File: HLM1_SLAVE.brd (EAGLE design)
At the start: 47.9 x 63.5 mm, 7 parts

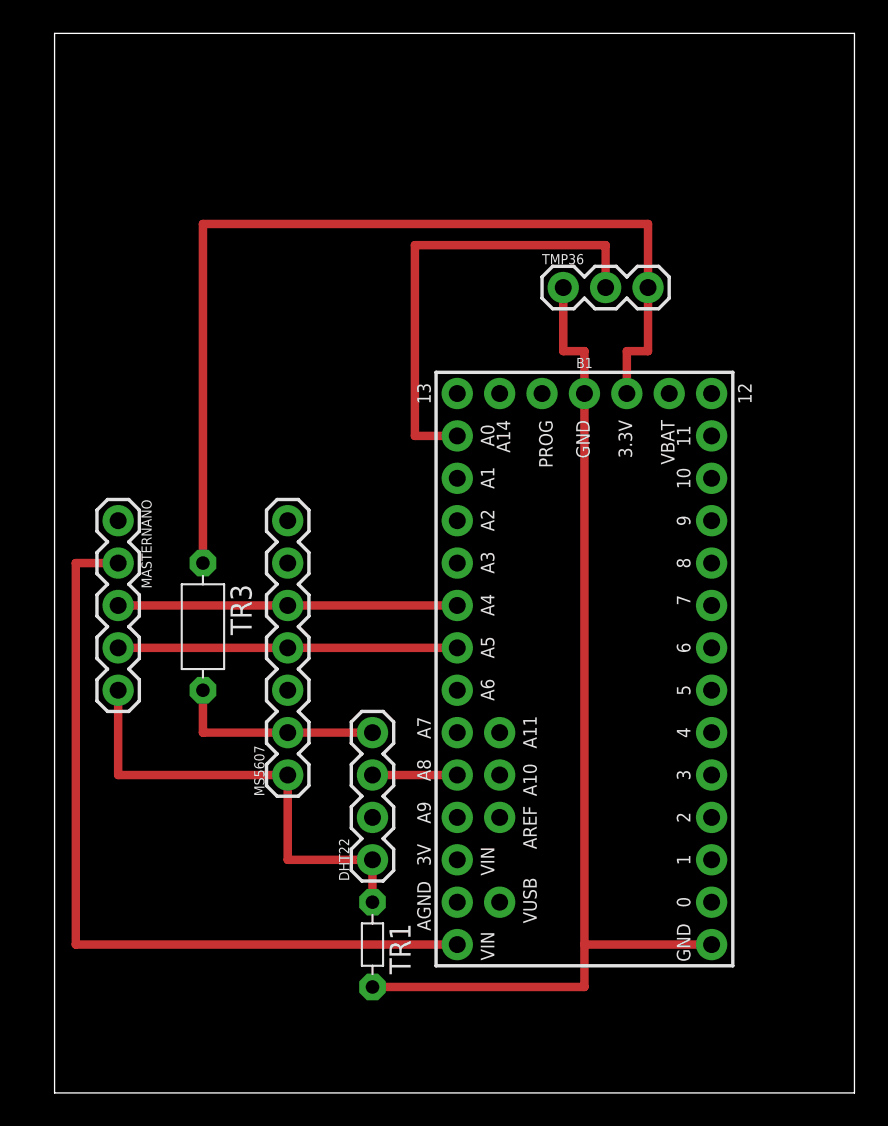
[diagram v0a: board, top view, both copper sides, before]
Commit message: Connected I2C lines to slave device for board carving
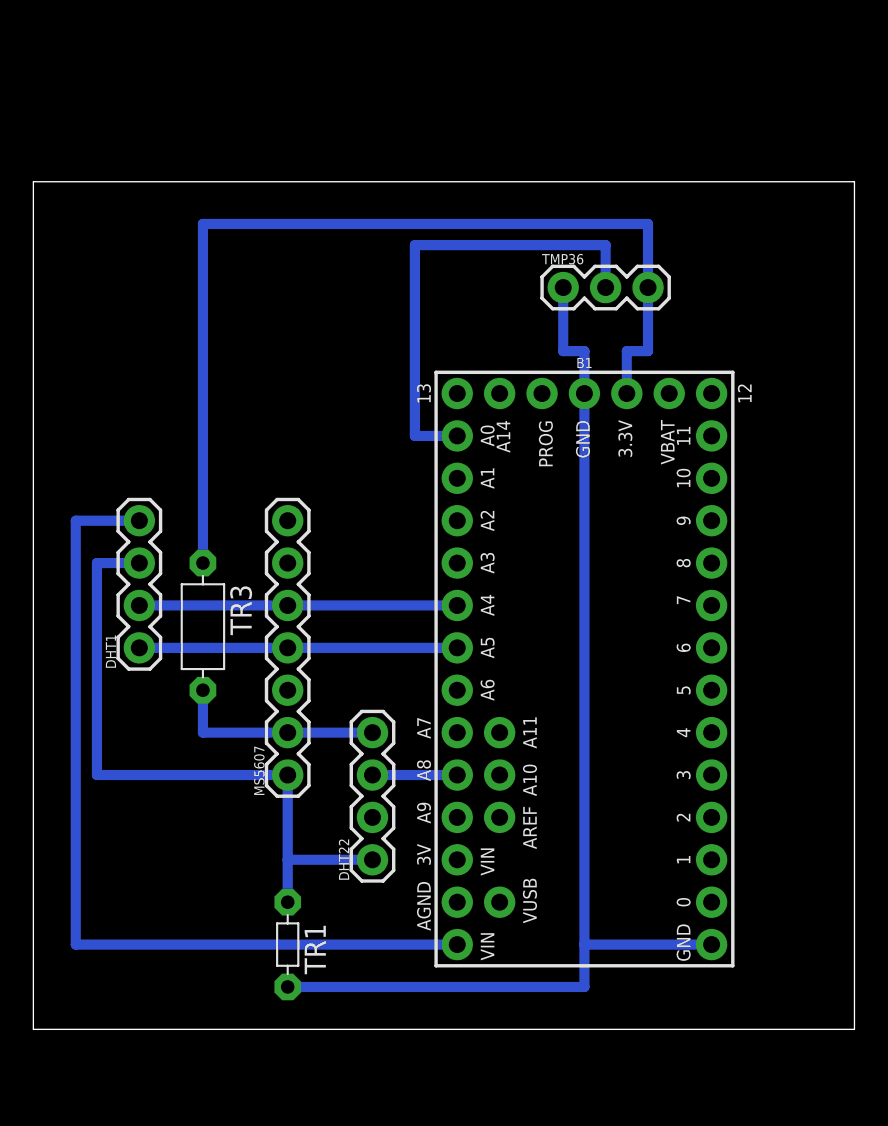
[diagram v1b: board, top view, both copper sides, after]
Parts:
- removed MASTERNANO: (no value), SparkFun-Connectors:1X05
- added DHT1: (no value), SparkFun-Connectors:1X04
- moved TR1 5.08 mm to (33.0, 16.5)
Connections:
- removed net 5V: MASTERNANO.1
- net GND: now also DHT1.3; no longer MASTERNANO.5
- net SCL: now also DHT1.1; no longer MASTERNANO.4
- net SDA: now also DHT1.2; no longer MASTERNANO.3
- net VIN: now also DHT1.4; no longer MASTERNANO.2
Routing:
- net GND: track 91.4 -> 107.9 mm
- net VIN: track 48.3 -> 52.1 mm
- net SDA: track 20.3 -> 19.1 mm
- net SCL: track 20.3 -> 19.1 mm
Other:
- board size 47.9 x 63.5 mm -> 49.2 x 50.8 mm
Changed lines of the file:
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@@
 <?xml version="1.0" encoding="utf-8"?>
 <!DOCTYPE eagle SYSTEM "eagle.dtd">
-<eagle version="8.5.1">
+<eagle version="9.0.1">
 <drawing>
 <settings>
@@
 <board>
 <plain>
-<wire x1="19.05" y1="7.62" x2="66.98" y2="7.62" width="0" layer="20"/>
-<wire x1="66.98" y1="7.62" x2="66.98" y2="71.11" width="0" layer="20"/>
-<wire x1="66.98" y1="71.11" x2="19.05" y2="71.11" width="0" layer="20"/>
-<wire x1="19.05" y1="71.11" x2="19.05" y2="7.62" width="0" layer="20"/>
+<wire x1="17.78" y1="11.43" x2="66.98" y2="11.43" width="0" layer="20"/>
+<wire x1="66.98" y1="11.43" x2="66.98" y2="62.22" width="0" layer="20"/>
+<wire x1="66.98" y1="62.22" x2="17.78" y2="62.22" width="0" layer="20"/>
+<wire x1="17.78" y1="62.22" x2="17.78" y2="11.43" width="0" layer="20"/>
 <text x="35.56" y="62.23" size="1.778" layer="27">+</text>
 </plain>
@@
 </element>
 <element name="MS5607" library="SparkFun-Connectors" package="1X07" value="" x="33.02" y="26.67" rot="R90"/>
-<element name="MASTERNANO" library="SparkFun-Connectors" package="1X05" value="" x="22.86" y="41.91" rot="R270"/>
-<element name="TR1" library="discrete" library_urn="urn:adsk.eagle:library:211" package="R-5" package3d_urn="urn:adsk.eagle:package:12931/1" value="" x="38.1" y="16.51" rot="R270"/>
+<element name="TR1" library="discrete" library_urn="urn:adsk.eagle:library:211" package="R-5" package3d_urn="urn:adsk.eagle:package:12931/1" value="" x="33.02" y="16.51" rot="R270"/>
 <element name="TR3" library="discrete" library_urn="urn:adsk.eagle:library:211" package="R-7,5" package3d_urn="urn:adsk.eagle:package:12930/1" value="" x="27.94" y="35.56" rot="R270"/>
+<element name="DHT1" library="SparkFun-Connectors" package="1X04" value="" x="24.13" y="34.29" rot="R90">
+<attribute name="PROD_ID" value="CONN-09696" x="24.13" y="34.29" size="1.778" layer="27" rot="R90" display="off"/>
+</element>
 </elements>
 <signals>
@@
 </signal>
 <signal name="GND">
-<contactref element="MASTERNANO" pad="5"/>
 <contactref element="DHT22" pad="1"/>
 <contactref element="B1" pad="GND"/>
@@
 <contactref element="MS5607" pad="1"/>
 <contactref element="B1" pad="GND1"/>
-<wire x1="49.53" y1="55.88" x2="49.53" y2="52.07" width="0.508" layer="1"/>
-<wire x1="49.53" y1="52.07" x2="50.8" y2="52.07" width="0.508" layer="1"/>
-<wire x1="50.8" y1="52.07" x2="50.8" y2="49.53" width="0.508" layer="1"/>
-<wire x1="38.1" y1="21.59" x2="33.02" y2="21.59" width="0.508" layer="1"/>
-<wire x1="33.02" y1="21.59" x2="33.02" y2="26.67" width="0.508" layer="1"/>
-<wire x1="33.02" y1="26.67" x2="22.86" y2="26.67" width="0.508" layer="1"/>
-<wire x1="22.86" y1="26.67" x2="22.86" y2="31.75" width="0.508" layer="1"/>
+<wire x1="49.53" y1="55.88" x2="49.53" y2="52.07" width="0.6096" layer="16"/>
+<wire x1="49.53" y1="52.07" x2="50.8" y2="52.07" width="0.6096" layer="16"/>
+<wire x1="50.8" y1="52.07" x2="50.8" y2="49.53" width="0.6096" layer="16"/>
+<wire x1="38.1" y1="21.59" x2="33.02" y2="21.59" width="0.6096" layer="16"/>
+<wire x1="33.02" y1="21.59" x2="33.02" y2="26.67" width="0.6096" layer="16"/>
 <contactref element="TR1" pad="2"/>
 <contactref element="TR1" pad="1"/>
-<wire x1="38.1" y1="21.59" x2="38.1" y2="19.05" width="0.508" layer="1"/>
-<wire x1="58.42" y1="16.51" x2="50.8" y2="16.51" width="0.508" layer="1"/>
-<wire x1="50.8" y1="16.51" x2="50.8" y2="49.53" width="0.508" layer="1"/>
-<wire x1="38.1" y1="13.97" x2="50.8" y2="13.97" width="0.508" layer="1"/>
-<wire x1="50.8" y1="13.97" x2="50.8" y2="16.51" width="0.508" layer="1"/>
-<wire x1="38.1" y1="19.05" x2="38.1" y2="13.97" width="0" layer="19" extent="1-1"/>
+<wire x1="58.42" y1="16.51" x2="50.8" y2="16.51" width="0.6096" layer="16"/>
+<wire x1="50.8" y1="16.51" x2="50.8" y2="49.53" width="0.6096" layer="16"/>
+<wire x1="33.02" y1="13.97" x2="50.8" y2="13.97" width="0.6096" layer="16"/>
+<wire x1="50.8" y1="13.97" x2="50.8" y2="16.51" width="0.6096" layer="16"/>
+<contactref element="DHT1" pad="3"/>
+<wire x1="21.59" y1="26.67" x2="21.59" y2="39.37" width="0.6096" layer="16"/>
+<wire x1="21.59" y1="39.37" x2="24.13" y2="39.37" width="0.6096" layer="16"/>
+<wire x1="33.02" y1="26.67" x2="21.59" y2="26.67" width="0.6096" layer="16"/>
+<wire x1="33.02" y1="19.05" x2="33.02" y2="21.59" width="0.6096" layer="16"/>
+<wire x1="33.02" y1="19.05" x2="33.02" y2="13.97" width="0" layer="19" extent="1-1"/>
 </signal>
 <signal name="SDA">
-<contactref element="MASTERNANO" pad="3"/>
+<contactref element="MS5607" pad="5"/>
+<contactref element="DHT1" pad="2"/>
+<wire x1="24.13" y1="36.83" x2="33.02" y2="36.83" width="0.6096" layer="16"/>
 <contactref element="B1" pad="18"/>
-<contactref element="MS5607" pad="5"/>
-<wire x1="33.02" y1="36.83" x2="43.18" y2="36.83" width="0.508" layer="1"/>
-<wire x1="22.86" y1="36.83" x2="33.02" y2="36.83" width="0.508" layer="1"/>
+<wire x1="33.02" y1="36.83" x2="43.18" y2="36.83" width="0.6096" layer="16"/>
 </signal>
 <signal name="SCL">
-<contactref element="MASTERNANO" pad="4"/>
+<contactref element="MS5607" pad="4"/>
+<contactref element="DHT1" pad="1"/>
+<wire x1="24.13" y1="34.29" x2="33.02" y2="34.29" width="0.6096" layer="16"/>
 <contactref element="B1" pad="19"/>
-<contactref element="MS5607" pad="4"/>
-<wire x1="33.02" y1="34.29" x2="43.18" y2="34.29" width="0.508" layer="1"/>
-<wire x1="22.86" y1="34.29" x2="33.02" y2="34.29" width="0.508" layer="1"/>
-</signal>
-<signal name="5V">
-<contactref element="MASTERNANO" pad="1"/>
+<wire x1="33.02" y1="34.29" x2="43.18" y2="34.29" width="0.6096" layer="16"/>
 </signal>
 <signal name="22">
 <contactref element="DHT22" pad="3"/>
 <contactref element="B1" pad="22"/>
-<wire x1="38.1" y1="26.67" x2="43.18" y2="26.67" width="0.508" layer="1"/>
+<wire x1="38.1" y1="26.67" x2="43.18" y2="26.67" width="0.6096" layer="16"/>
 </signal>
 <signal name="A0">
 <contactref element="TMP36" pad="2"/>
 <contactref element="B1" pad="14"/>
-<wire x1="52.07" y1="55.88" x2="52.07" y2="58.42" width="0.508" layer="1"/>
-<wire x1="52.07" y1="58.42" x2="40.64" y2="58.42" width="0.508" layer="1"/>
-<wire x1="40.64" y1="58.42" x2="40.64" y2="46.99" width="0.508" layer="1"/>
-<wire x1="40.64" y1="46.99" x2="43.18" y2="46.99" width="0.508" layer="1"/>
+<wire x1="52.07" y1="55.88" x2="52.07" y2="58.42" width="0.6096" layer="16"/>
+<wire x1="52.07" y1="58.42" x2="40.64" y2="58.42" width="0.6096" layer="16"/>
+<wire x1="40.64" y1="58.42" x2="40.64" y2="46.99" width="0.6096" layer="16"/>
+<wire x1="40.64" y1="46.99" x2="43.18" y2="46.99" width="0.6096" layer="16"/>
 </signal>
 <signal name="3V3">
@@
 <contactref element="TMP36" pad="3"/>
 <contactref element="DHT22" pad="4"/>
-<wire x1="54.61" y1="55.88" x2="54.61" y2="52.07" width="0.508" layer="1"/>
-<wire x1="53.34" y1="52.07" x2="54.61" y2="52.07" width="0.508" layer="1"/>
-<wire x1="53.34" y1="49.53" x2="53.34" y2="52.07" width="0.508" layer="1"/>
+<wire x1="54.61" y1="55.88" x2="54.61" y2="52.07" width="0.6096" layer="16"/>
+<wire x1="53.34" y1="52.07" x2="54.61" y2="52.07" width="0.6096" layer="16"/>
+<wire x1="53.34" y1="49.53" x2="53.34" y2="52.07" width="0.6096" layer="16"/>
 <contactref element="MS5607" pad="2"/>
 <contactref element="TR3" pad="1"/>
 <contactref element="TR3" pad="2"/>
-<wire x1="33.02" y1="29.21" x2="27.94" y2="29.21" width="0.508" layer="1"/>
-<wire x1="27.94" y1="29.21" x2="27.94" y2="31.75" width="0.508" layer="1"/>
-<wire x1="38.1" y1="29.21" x2="33.02" y2="29.21" width="0.508" layer="1"/>
-<wire x1="54.61" y1="55.88" x2="54.61" y2="59.69" width="0.508" layer="1"/>
-<wire x1="54.61" y1="59.69" x2="27.94" y2="59.69" width="0.508" layer="1"/>
-<wire x1="27.94" y1="59.69" x2="27.94" y2="39.37" width="0.508" layer="1"/>
+<wire x1="33.02" y1="29.21" x2="27.94" y2="29.21" width="0.6096" layer="16"/>
+<wire x1="27.94" y1="29.21" x2="27.94" y2="31.75" width="0.6096" layer="16"/>
+<wire x1="38.1" y1="29.21" x2="33.02" y2="29.21" width="0.6096" layer="16"/>
+<wire x1="54.61" y1="55.88" x2="54.61" y2="59.69" width="0.6096" layer="16"/>
+<wire x1="54.61" y1="59.69" x2="27.94" y2="59.69" width="0.6096" layer="16"/>
+<wire x1="27.94" y1="59.69" x2="27.94" y2="39.37" width="0.6096" layer="16"/>
 <wire x1="27.94" y1="31.75" x2="27.94" y2="39.37" width="0" layer="19" extent="1-1"/>
 </signal>
 <signal name="VIN">
 <contactref element="B1" pad="VIN"/>
-<contactref element="MASTERNANO" pad="2"/>
-<wire x1="22.86" y1="39.37" x2="20.32" y2="39.37" width="0.508" layer="1"/>
-<wire x1="20.32" y1="39.37" x2="20.32" y2="16.51" width="0.508" layer="1"/>
-<wire x1="20.32" y1="16.51" x2="43.18" y2="16.51" width="0.508" layer="1"/>
+<wire x1="20.32" y1="16.51" x2="43.18" y2="16.51" width="0.6096" layer="16"/>
+<contactref element="DHT1" pad="4"/>
+<wire x1="24.13" y1="41.91" x2="20.32" y2="41.91" width="0.6096" layer="16"/>
+<wire x1="20.32" y1="41.91" x2="20.32" y2="16.51" width="0.6096" layer="16"/>
 </signal>
 </signals>

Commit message: Improved routing
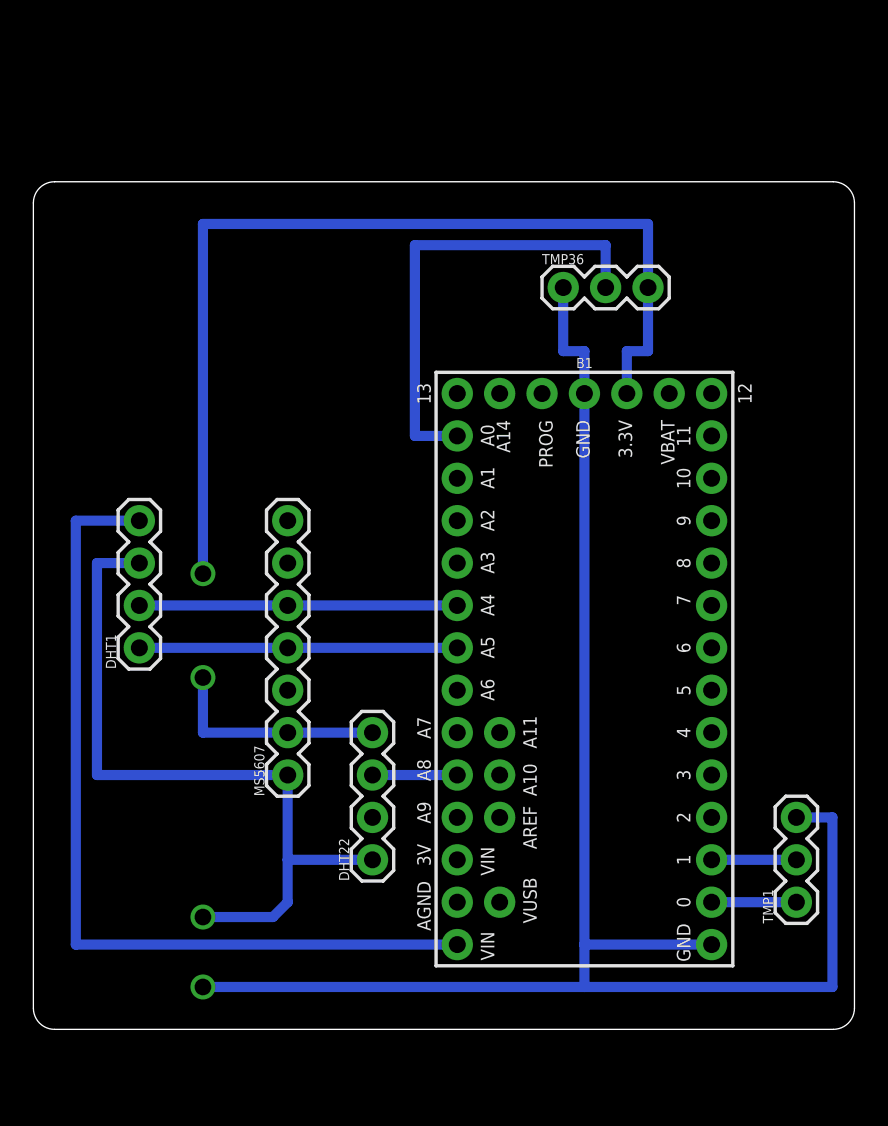
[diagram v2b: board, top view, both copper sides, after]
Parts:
- removed TR1: (no value), discrete:R-5
- removed TR3: (no value), discrete:R-7,5
- added TMP1: (no value), SparkFun-Connectors:1X03
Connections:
- new net N$1: B1.0, TMP1.1
- new net N$2: B1.1, TMP1.2
- net 3V3: no longer TR3.1, TR3.2
- net GND: now also TMP1.3; no longer TR1.1, TR1.2
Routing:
- net GND: track 107.9 -> 145.7 mm, vias 0 -> 2
- net N$2: track 0.00 -> 5.08 mm
- net N$1: track 0.00 -> 5.08 mm
- net 3V3: track 71.1 -> 72.5 mm, vias 0 -> 2
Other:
- outline, holes or cut-outs redrawn
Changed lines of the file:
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@@
 <board>
 <plain>
-<wire x1="17.78" y1="11.43" x2="66.98" y2="11.43" width="0" layer="20"/>
-<wire x1="66.98" y1="11.43" x2="66.98" y2="62.22" width="0" layer="20"/>
-<wire x1="66.98" y1="62.22" x2="17.78" y2="62.22" width="0" layer="20"/>
-<wire x1="17.78" y1="62.22" x2="17.78" y2="11.43" width="0" layer="20"/>
+<wire x1="17.78" y1="60.95" x2="17.78" y2="12.7" width="0" layer="20"/>
+<wire x1="17.78" y1="12.7" x2="19.05" y2="11.43" width="0" layer="20" curve="90"/>
+<wire x1="19.05" y1="11.43" x2="65.71" y2="11.43" width="0" layer="20"/>
+<wire x1="65.71" y1="11.43" x2="66.98" y2="12.7" width="0" layer="20" curve="90"/>
+<wire x1="66.98" y1="12.7" x2="66.98" y2="60.95" width="0" layer="20"/>
+<wire x1="66.98" y1="60.95" x2="65.71" y2="62.22" width="0" layer="20" curve="90"/>
+<wire x1="65.71" y1="62.22" x2="19.05" y2="62.22" width="0" layer="20"/>
+<wire x1="19.05" y1="62.22" x2="17.78" y2="60.95" width="0" layer="20" curve="90"/>
 <text x="35.56" y="62.23" size="1.778" layer="27">+</text>
 </plain>
@@
 </element>
 <element name="MS5607" library="SparkFun-Connectors" package="1X07" value="" x="33.02" y="26.67" rot="R90"/>
-<element name="TR1" library="discrete" library_urn="urn:adsk.eagle:library:211" package="R-5" package3d_urn="urn:adsk.eagle:package:12931/1" value="" x="33.02" y="16.51" rot="R270"/>
-<element name="TR3" library="discrete" library_urn="urn:adsk.eagle:library:211" package="R-7,5" package3d_urn="urn:adsk.eagle:package:12930/1" value="" x="27.94" y="35.56" rot="R270"/>
 <element name="DHT1" library="SparkFun-Connectors" package="1X04" value="" x="24.13" y="34.29" rot="R90">
 <attribute name="PROD_ID" value="CONN-09696" x="24.13" y="34.29" size="1.778" layer="27" rot="R90" display="off"/>
+</element>
+<element name="TMP1" library="SparkFun-Connectors" package="1X03" value="" x="63.5" y="19.05" rot="R90">
+<attribute name="PROD_ID" value="XXX-00000" x="63.5" y="19.05" size="1.778" layer="27" rot="R90" display="off"/>
 </element>
 </elements>
@@
 <wire x1="38.1" y1="21.59" x2="33.02" y2="21.59" width="0.6096" layer="16"/>
 <wire x1="33.02" y1="21.59" x2="33.02" y2="26.67" width="0.6096" layer="16"/>
-<contactref element="TR1" pad="2"/>
-<contactref element="TR1" pad="1"/>
 <wire x1="58.42" y1="16.51" x2="50.8" y2="16.51" width="0.6096" layer="16"/>
 <wire x1="50.8" y1="16.51" x2="50.8" y2="49.53" width="0.6096" layer="16"/>
-<wire x1="33.02" y1="13.97" x2="50.8" y2="13.97" width="0.6096" layer="16"/>
-<wire x1="50.8" y1="13.97" x2="50.8" y2="16.51" width="0.6096" layer="16"/>
+<wire x1="50.8" y1="16.51" x2="50.8" y2="13.97" width="0.6096" layer="16"/>
 <contactref element="DHT1" pad="3"/>
 <wire x1="21.59" y1="26.67" x2="21.59" y2="39.37" width="0.6096" layer="16"/>
 <wire x1="21.59" y1="39.37" x2="24.13" y2="39.37" width="0.6096" layer="16"/>
 <wire x1="33.02" y1="26.67" x2="21.59" y2="26.67" width="0.6096" layer="16"/>
+<via x="27.94" y="18.161" extent="1-16" drill="1"/>
+<via x="27.94" y="13.97" extent="1-16" drill="1"/>
+<wire x1="50.8" y1="13.97" x2="27.94" y2="13.97" width="0.6096" layer="16"/>
+<contactref element="TMP1" pad="3"/>
+<wire x1="50.8" y1="13.97" x2="65.6592" y2="13.97" width="0.6096" layer="16"/>
+<wire x1="65.6592" y1="13.97" x2="65.6592" y2="24.13" width="0.6096" layer="16"/>
+<wire x1="65.6592" y1="24.13" x2="63.5" y2="24.13" width="0.6096" layer="16"/>
+<wire x1="27.94" y1="18.161" x2="32.131" y2="18.161" width="0.6096" layer="16"/>
+<wire x1="32.131" y1="18.161" x2="33.02" y2="19.05" width="0.6096" layer="16"/>
 <wire x1="33.02" y1="19.05" x2="33.02" y2="21.59" width="0.6096" layer="16"/>
-<wire x1="33.02" y1="19.05" x2="33.02" y2="13.97" width="0" layer="19" extent="1-1"/>
+<wire x1="27.94" y1="13.97" x2="27.94" y2="18.161" width="0" layer="19" extent="1-1"/>
 </signal>
 <signal name="SDA">
@@
 <wire x1="53.34" y1="49.53" x2="53.34" y2="52.07" width="0.6096" layer="16"/>
 <contactref element="MS5607" pad="2"/>
-<contactref element="TR3" pad="1"/>
-<contactref element="TR3" pad="2"/>
-<wire x1="33.02" y1="29.21" x2="27.94" y2="29.21" width="0.6096" layer="16"/>
-<wire x1="27.94" y1="29.21" x2="27.94" y2="31.75" width="0.6096" layer="16"/>
+<wire x1="27.94" y1="29.21" x2="33.02" y2="29.21" width="0.6096" layer="16"/>
 <wire x1="38.1" y1="29.21" x2="33.02" y2="29.21" width="0.6096" layer="16"/>
 <wire x1="54.61" y1="55.88" x2="54.61" y2="59.69" width="0.6096" layer="16"/>
 <wire x1="54.61" y1="59.69" x2="27.94" y2="59.69" width="0.6096" layer="16"/>
-<wire x1="27.94" y1="59.69" x2="27.94" y2="39.37" width="0.6096" layer="16"/>
-<wire x1="27.94" y1="31.75" x2="27.94" y2="39.37" width="0" layer="19" extent="1-1"/>
+<wire x1="27.94" y1="59.69" x2="27.94" y2="38.735" width="0.6096" layer="16"/>
+<via x="27.94" y="38.735" extent="1-16" drill="1"/>
+<via x="27.94" y="32.512" extent="1-16" drill="1"/>
+<wire x1="27.94" y1="32.512" x2="27.94" y2="29.21" width="0.6096" layer="16"/>
+<wire x1="27.94" y1="32.512" x2="27.94" y2="38.735" width="0" layer="19" extent="16-16"/>
 </signal>
 <signal name="VIN">
@@
 <wire x1="20.32" y1="41.91" x2="20.32" y2="16.51" width="0.6096" layer="16"/>
 </signal>
+<signal name="N$1">
+<contactref element="B1" pad="0"/>
+<contactref element="TMP1" pad="1"/>
+<wire x1="63.5" y1="19.05" x2="58.42" y2="19.05" width="0.6096" layer="16"/>
+</signal>
+<signal name="N$2">
+<contactref element="B1" pad="1"/>
+<contactref element="TMP1" pad="2"/>
+<wire x1="58.42" y1="21.59" x2="63.5" y2="21.59" width="0.6096" layer="16"/>
+</signal>
 </signals>
 </board>
 </drawing>
-<compatibility>
-<note version="8.2" severity="warning">
-Since Version 8.2, EAGLE supports online libraries. The ids
-of those online libraries will not be understood (or retained)
-with this version.
-</note>
-<note version="8.3" severity="warning">
-Since Version 8.3, EAGLE supports URNs for individual library
-assets (packages, symbols, and devices). The URNs of those assets
-will not be understood (or retained) with this version.
-</note>
-<note version="8.3" severity="warning">
-Since Version 8.3, EAGLE supports the association of 3D packages
-with devices in libraries, schematics, and board files. Those 3D
-packages will not be understood (or retained) with this version.
-</note>
-</compatibility>
 </eagle>
